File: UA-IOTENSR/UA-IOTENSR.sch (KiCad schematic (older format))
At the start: 2 parts, among them SW1 SW_MEC_5G, U1 ESP32-S2-WROOM

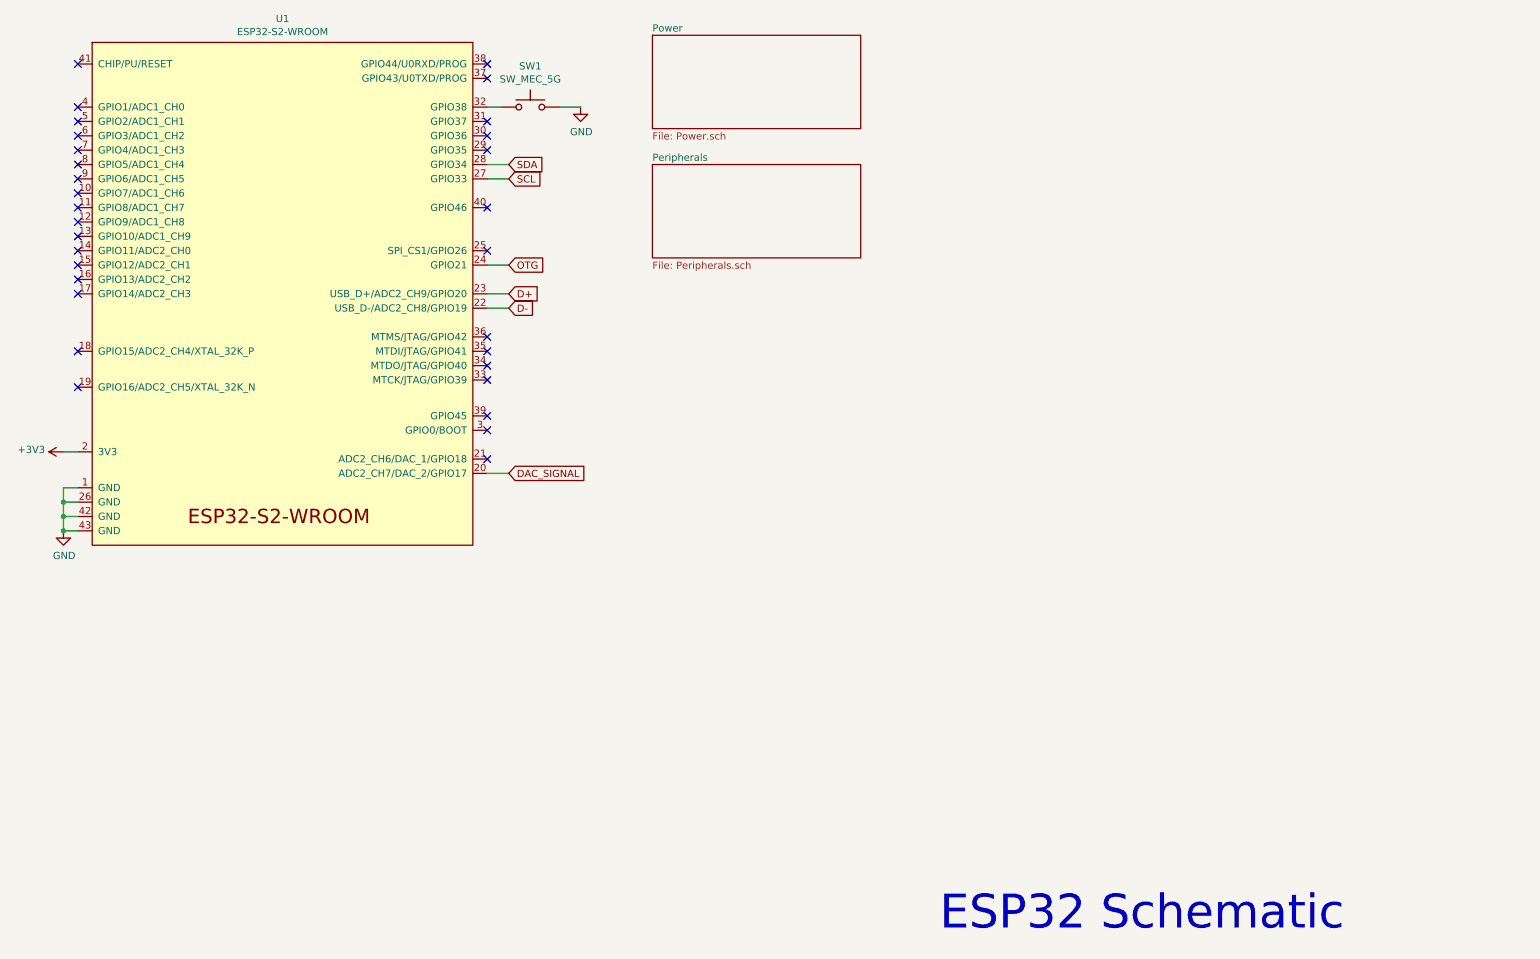
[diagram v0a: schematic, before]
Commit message: Reassessed components
Removed bar graph led array and lm3914
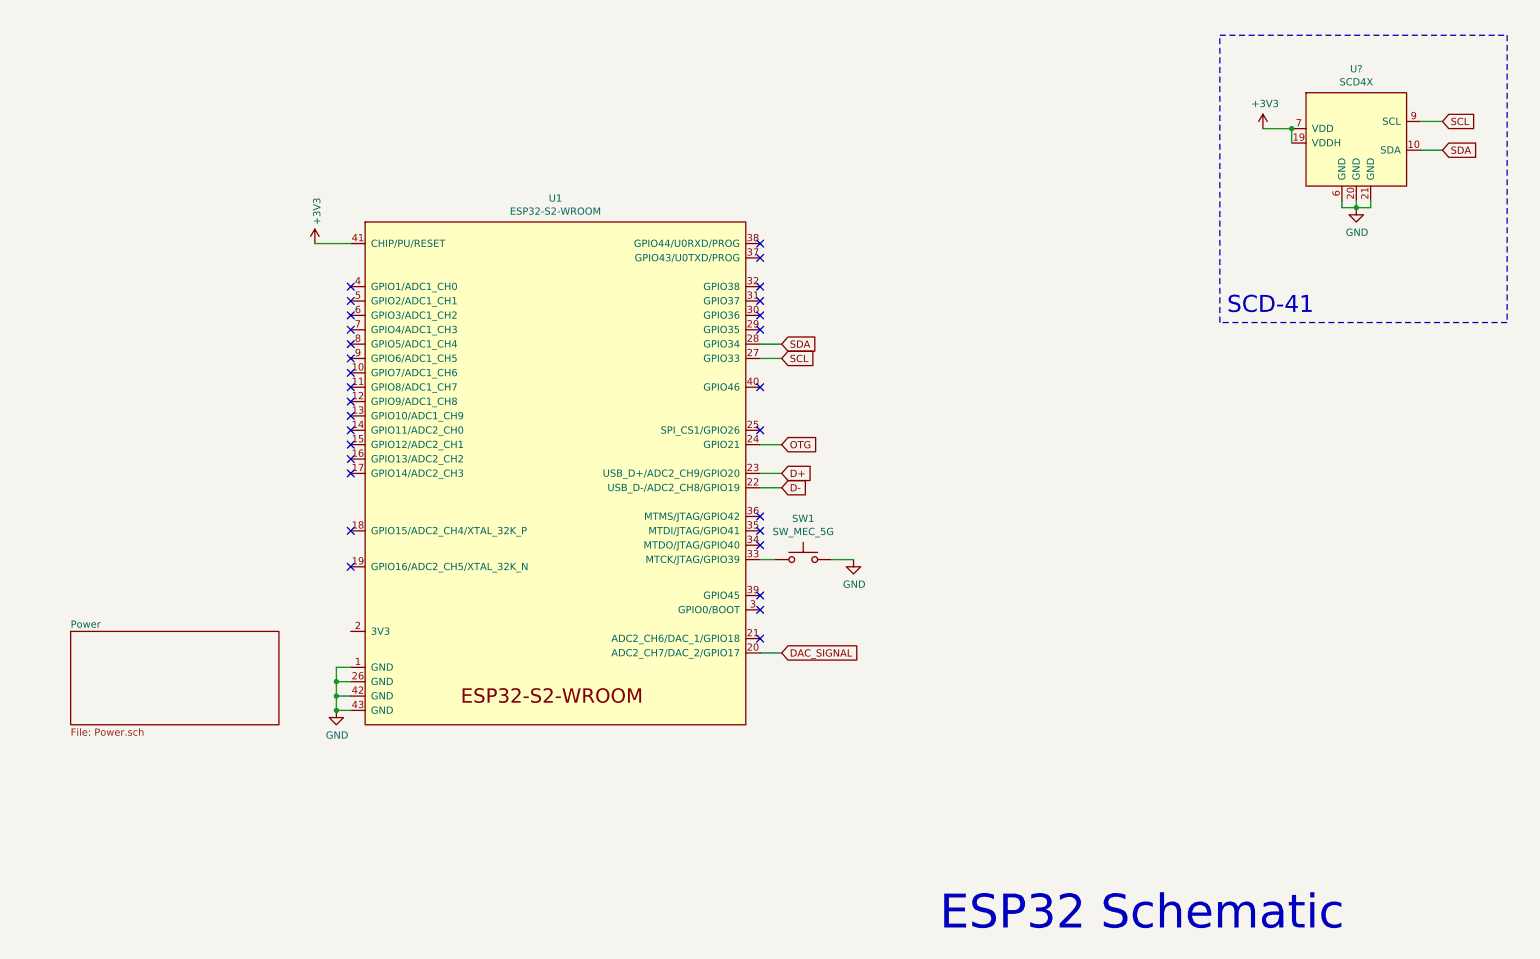
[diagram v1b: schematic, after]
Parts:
- added U?: SCD4X, symbol SCD4X:SCD4X
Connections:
- net +3V3: now also U1.41 (CHIP/PU/RESET), U?.19 (VDDH), U?.7 (VDD); no longer U1.2 (3V3)
- net GND: now also U?.20 (GND), U?.21 (GND), U?.6 (GND)
- net SCL: now also U?.9 (SCL)
- net SDA: now also U?.10 (SDA)
- net at SW1.1 (A), SW1.2 (A): now also U1.33 (MTCK/JTAG/GPIO39); no longer U1.32 (GPIO38)
- no-connect marks 31 -> 30
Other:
- note added: "SCD-41"
- moved on the sheet: SW1, U1

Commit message: Adding the LED Schematic
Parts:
- added LED?: APTF1616SURKCGKSYKC, KPTF1616RGBC11, symbol Samacs:APTF1616SURKCGKSYKC
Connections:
- net labels added: CATHODE_G, CATHODE_R, CATHODE_Y
- wire segments 25 -> 31
- no-connect marks 30 -> 27
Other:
- note added: "LED"
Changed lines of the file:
@@
 NoConn ~ 5750 4750
 NoConn ~ 5750 4650
-NoConn ~ 5750 2500
 NoConn ~ 5750 4300
 NoConn ~ 5750 4200
@@
 NoConn ~ 5750 3200
 NoConn ~ 5750 2800
-NoConn ~ 5750 2700
-NoConn ~ 5750 2600
 NoConn ~ 5750 2300
 NoConn ~ 5750 2200
@@
 	8950 750  10950 750
 Wire Notes Line
+	10950 2750 8950 2750
+Text Notes 9000 2700 0    118  ~ 0
+SCD-41
+$Comp
+L Samacs:APTF1616SURKCGKSYKC LED?
+U 1 1 61AF43CE
+P 9200 4050
+F 0 "LED?" H 9875 4315 50  0000 C CNN
+F 1 "APTF1616SURKCGKSYKC" H 9875 4224 50  0000 C CNN
+F 2 "KPTF1616RGBC11" H 10950 4150 50  0001 L CNN
+F 3 "" H 9150 3850 50  0001 L CNN
+F 4 "Standard LEDs - SMD RGY 1616 SMD" H 11150 3850 50  0001 L CNN "Description"
+F 5 "0.9" H 11150 3750 50  0001 L CNN "Height"
+F 6 "604-APTF1616KCGKSYKC" H 11150 3650 50  0001 L CNN "Mouser Part Number"
+F 7 "https://www.mouser.co.uk/ProductDetail/Kingbright/APTF1616SURKCGKSYKC?qs=FESYatJ8odK7UleJtP4p0g%3D%3D" H 11350 3550 50  0001 L CNN "Mouser Price/Stock"
+F 8 "Kingbright" H 11350 3450 50  0001 L CNN "Manufacturer_Name"
+F 9 "APTF1616SURKCGKSYKC" H 11350 3350 50  0001 L CNN "Manufacturer_Part_Number"
+	1    9200 4050
+	1    0    0    -1
+$EndComp
+Text Notes 8200 4950 0    118  ~ 0
+LED
+Wire Notes Line
+	8950 2750 8950 750
+Wire Notes Line
 	10950 750  10950 2750
 Wire Notes Line
-	10950 2750 8950 2750
+	11100 5000 11100 3450
 Wire Notes Line
-	8950 2750 8950 750
-Text Notes 9000 2700 0    118  ~ 0
-SCD-41
+	8150 3450 8150 5000
+Wire Wire Line
+	5750 2600 5900 2600
+Text GLabel 5900 2600 2    50   Input ~ 0
+CATHODE_G
+Text GLabel 5900 2500 2    50   Input ~ 0
+CATHODE_R
+Wire Wire Line
+	5750 2500 5900 2500
+Wire Wire Line
+	5750 2700 5900 2700
+Text GLabel 5900 2700 2    50   Input ~ 0
+CATHODE_Y
+Wire Wire Line
+	9000 4150 8850 4150
+Text GLabel 8850 4150 0    50   Input ~ 0
+CATHODE_G
+Text GLabel 8850 4050 0    50   Input ~ 0
+CATHODE_R
+Wire Wire Line
+	9000 4050 8850 4050
+Wire Wire Line
+	9000 4250 8850 4250
+Text GLabel 8850 4250 0    50   Input ~ 0
+CATHODE_Y
+$Comp
+L power:GND #PWR?
+U 1 1 61AFFCA4
+P 10750 4150
+F 0 "#PWR?" H 10750 3900 50  0001 C CNN
+F 1 "GND" H 10755 3977 50  0000 C CNN
+F 2 "" H 10750 4150 50  0001 C CNN
+F 3 "" H 10750 4150 50  0001 C CNN
+	1    10750 4150
+	1    0    0    -1
+$EndComp
+Wire Notes Line
+	8150 3450 11100 3450
+Wire Notes Line
+	8150 5000 11100 5000
 $EndSCHEMATC

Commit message: Reworking Power Schematic page for the change to NiMH tech
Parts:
- gave numbers to parts that had none: 2
- renumbered SW1 to SW101, U1 to U101
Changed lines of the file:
@@
 $EndDescr
 $Comp
-L power:GND #PWR01
+L power:GND #PWR0102
 U 1 1 61961638
 P 2800 5450
-F 0 "#PWR01" H 2800 5200 50  0001 C CNN
+F 0 "#PWR0102" H 2800 5200 50  0001 C CNN
 F 1 "GND" H 2805 5277 50  0000 C CNN
 F 2 "" H 2800 5450 50  0001 C CNN
@@
 	2800 5450 2900 5450
 $Comp
-L Espressif:ESP32-S2-WROOM U1
+L Espressif:ESP32-S2-WROOM U101
 U 1 1 619E5D94
 P 4300 3800
-F 0 "U1" H 4325 5715 50  0000 C CNN
+F 0 "U101" H 4325 5715 50  0000 C CNN
 F 1 "ESP32-S2-WROOM" H 4325 5624 50  0000 C CNN
 F 2 "Espressif:ESP32-S2-WROOM" H 4300 1900 50  0001 C CNN
@@
 	6250 4400 6400 4400
 $Comp
-L Switch:SW_MEC_5G SW1
+L Switch:SW_MEC_5G SW101
 U 1 1 619D98CD
 P 6050 4400
-F 0 "SW1" H 6050 4685 50  0000 C CNN
+F 0 "SW101" H 6050 4685 50  0000 C CNN
 F 1 "SW_MEC_5G" H 6050 4594 50  0000 C CNN
 F 2 "" H 6050 4600 50  0001 C CNN
@@
 	5750 4400 5850 4400
 $Comp
-L power:GND #PWR02
+L power:GND #PWR0103
 U 1 1 61A04BEB
 P 6400 4400
-F 0 "#PWR02" H 6400 4150 50  0001 C CNN
+F 0 "#PWR0103" H 6400 4150 50  0001 C CNN
 F 1 "GND" H 6405 4227 50  0000 C CNN
 F 2 "" H 6400 4400 50  0001 C CNN
@@
 ESP32 Schematic
 $Comp
-L power:+3V3 #PWR06
+L power:+3V3 #PWR0101
 U 1 1 61A18D2A
 P 2650 2200
-F 0 "#PWR06" H 2650 2050 50  0001 C CNN
+F 0 "#PWR0101" H 2650 2050 50  0001 C CNN
 F 1 "+3V3" V 2665 2328 50  0000 L CNN
 F 2 "" H 2650 2200 50  0001 C CNN
@@
 	2900 2200 2650 2200
 $Comp
-L SCD4X:SCD4X U?
+L SCD4X:SCD4X U102
 U 1 1 61B02C43
 P 9900 1450
-AR Path="/61B02C43" Ref="U?"  Part="1"
+AR Path="/61B02C43" Ref="U102"  Part="1"
 AR Path="/61A1DC3C/61B02C43" Ref="U?"  Part="1"
-F 0 "U?" H 9900 1915 50  0000 C CNN
+F 0 "U102" H 9900 1915 50  0000 C CNN
 F 1 "SCD4X" H 9900 1824 50  0000 C CNN
 F 2 "" H 9900 1900 50  0001 C CNN
@@
 	9900 1950 10000 1950
 $Comp
-L power:GND #PWR?
+L power:GND #PWR0105
 U 1 1 61B02C53
 P 9900 1950
-AR Path="/61B02C53" Ref="#PWR?"  Part="1"
+AR Path="/61B02C53" Ref="#PWR0105"  Part="1"
 AR Path="/61A1DC3C/61B02C53" Ref="#PWR?"  Part="1"
-F 0 "#PWR?" H 9900 1700 50  0001 C CNN
+F 0 "#PWR0105" H 9900 1700 50  0001 C CNN
 F 1 "GND" H 9905 1777 50  0000 C CNN
 F 2 "" H 9900 1950 50  0001 C CNN
@@
 Connection ~ 9450 1400
 $Comp
-L power:+3V3 #PWR?
+L power:+3V3 #PWR0104
 U 1 1 61B02C5C
 P 9250 1400
-F 0 "#PWR?" H 9250 1250 50  0001 C CNN
+F 0 "#PWR0104" H 9250 1250 50  0001 C CNN
 F 1 "+3V3" H 9265 1573 50  0000 C CNN
 F 2 "" H 9250 1400 50  0001 C CNN
@@
 SCD-41
 $Comp
-L Samacs:APTF1616SURKCGKSYKC LED?
+L Samacs:APTF1616SURKCGKSYKC LED101
 U 1 1 61AF43CE
 P 9200 4050
-F 0 "LED?" H 9875 4315 50  0000 C CNN
+F 0 "LED101" H 9875 4315 50  0000 C CNN
 F 1 "APTF1616SURKCGKSYKC" H 9875 4224 50  0000 C CNN
 F 2 "KPTF1616RGBC11" H 10950 4150 50  0001 L CNN
@@
 CATHODE_Y
 $Comp
-L power:GND #PWR?
+L power:GND #PWR0106
 U 1 1 61AFFCA4
 P 10750 4150
-F 0 "#PWR?" H 10750 3900 50  0001 C CNN
+F 0 "#PWR0106" H 10750 3900 50  0001 C CNN
 F 1 "GND" H 10755 3977 50  0000 C CNN
 F 2 "" H 10750 4150 50  0001 C CNN

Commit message: Updates to power schematic
Updated LED Resistor Value
Updated Page Title
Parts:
- LED101: symbol Samacs:APTF1616SURKCGKSYKC -> UA-IOTENSR-rescue:APTF1616SURKCGKSYKC-Samacs
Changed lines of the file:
@@
 OTG
 $Sheet
-S 950  4900 1450 650
+S 900  4850 1450 650
 U 61A2F8E2
 F0 "Power" 50
@@
 SCD-41
 $Comp
-L Samacs:APTF1616SURKCGKSYKC LED101
+L UA-IOTENSR-rescue:APTF1616SURKCGKSYKC-Samacs LED101
 U 1 1 61AF43CE
 P 9200 4050
